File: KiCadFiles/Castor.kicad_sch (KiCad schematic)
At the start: 0 parts

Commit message: Update KiCad project files for Castor: added 3D viewports, IPC2581 settings, and enhanced ERC configurations. Updated schematic with new USB-C and audio jack components, including detailed properties and footprints. Improved net settings and added additional components for better functionality.
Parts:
- added C1, C10, C11, C12, C14, C2, C3, C4, C8, C9: 100nF, Capacitor_SMD:C_0402_1005Metric, symbol Device:C
- added C13, C5: 10uF, Capacitor_SMD:C_0402_1005Metric, symbol Device:C
- added C15, C16, C6, C7: 1uF, Capacitor_SMD:C_0402_1005Metric, symbol Device:C
- added F1, F2: 500mA, Fuse:Fuse_1206_3216Metric, symbol Device:Polyfuse_Small
- added J1, J2: USB_C_Receptacle_USB2.0_14P, Connector_USB:USB_C_Receptacle_HRO_TYPE-C-31-M-12, symbol Connector:USB_C_Receptacle_USB2.0_14P
- added J3: TRRS-L, Connector_Audio:Jack_3.5mm_PJ320E_Horizontal, symbol Connector_Audio:AudioJack4
- added J4: TRRS-R, Connector_Audio:Jack_3.5mm_PJ320E_Horizontal, symbol Connector_Audio:AudioJack4
- added R1, R2, R3, R5: 5.1k, Resistor_SMD:R_0402_1005Metric, symbol Device:R
- added R4, R6: 10k, Resistor_SMD:R_0402_1005Metric, symbol Device:R
- added SW1, SW2, SW3, SW4: SW_DPST_x2, Button_Switch_SMD:SW_Push_1P1T_XKB_TS-1187A, symbol Switch:SW_DPST_x2
- added U1, U5: XC6206PxxxMR, Package_TO_SOT_SMD:SOT-23-3, symbol Regulator_Linear:XC6206PxxxMR
- added U2, U4: STM32F072CBTx, Package_QFP:LQFP-48_7x7mm_P0.5mm, symbol MCU_ST_STM32F0:STM32F072CBTx
- added U3, U6: SRV05-4, Package_TO_SOT_SMD:SOT-23-6, symbol Power_Protection:SRV05-4
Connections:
- new net: J2.A5 (CC1), R5.1
- new net: J2.B5 (CC2), R3.1
- new net: J1.B5 (CC2), R1.1
- new net: J1.A5 (CC1), R2.1
- new net +3V3: C1.1, C10.1, C11.1, C12.1, C13.1, C16.1, C2.1, C3.1, C4.1, C5.1, C7.1, C9.1, J3.S, J4.S, SW2.2 (B), SW4.2 (B), U1.2 (VO), U2.1 (VBAT), U2.24 (VDD), U2.36 (VDDIO2), U2.48 (VDD), U2.9 (VDDA), U4.1 (VBAT), U4.24 (VDD), U4.36 (VDDIO2), U4.48 (VDD), U4.9 (VDDA), U5.2 (VO)
- new net +5V: C15.1, C6.1, F1.2, F2.2, U1.3 (VI), U3.5 (VP), U5.3 (VI), U6.5 (VP)
- new net BOOT-1: R4.1, R6.1, SW2.1 (A), SW4.1 (A), U2.44 (BOOT0), U4.44 (BOOT0)
- new net DN: J1.A7 (D-), J1.B7 (D-), J2.A7 (D-), J2.B7 (D-), U2.32 (PA11), U3.4 (IO3), U4.32 (PA11), U6.4 (IO3)
- new net DP: J1.A6 (D+), J1.B6 (D+), J2.A6 (D+), J2.B6 (D+), U2.33 (PA12), U3.6 (IO4), U4.33 (PA12), U6.6 (IO4)
- new net GND: C1.2, C10.2, C11.2, C12.2, C13.2, C14.2, C15.2, C16.2, C2.2, C3.2, C4.2, C5.2, C6.2, C7.2, C8.2, C9.2, J1.A1 (GND), J1.A12 (GND), J1.B1 (GND), J1.B12 (GND), J2.A1 (GND), J2.A12 (GND), J2.B1 (GND), J2.B12 (GND), J3.R2, J4.R2, R1.2, R2.2, R3.2, R4.2, R5.2, R6.2, SW1.2 (B), SW3.2 (B), U1.1 (GND), U2.23 (VSS), U2.35 (VSS), U2.47 (VSS), U2.8 (VSSA), U3.2 (VN), U4.23 (VSS), U4.35 (VSS), U4.47 (VSS), U4.8 (VSSA), U5.1 (GND), U6.2 (VN)
- new net GNDREF: J1.S1 (SHIELD), J2.S1 (SHIELD)
- new net RST-1: C14.1, C8.1, SW1.1 (A), SW3.1 (A), U2.7 (NRST), U4.7 (NRST)
- new net USART2_RX: J3.R1, J4.T, U2.13 (PA3), U4.13 (PA3)
- new net USART2_TX: J3.T, J4.R1, U2.12 (PA2), U4.12 (PA2)
- new net VBUS: F1.1, F2.1, J1.A4 (VBUS), J1.A9 (VBUS), J1.B4 (VBUS), J1.B9 (VBUS), J2.A4 (VBUS), J2.A9 (VBUS), J2.B4 (VBUS), J2.B9 (VBUS)
- no-connect marks 0 -> 6
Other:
- note added: "Boot Switch"
- note added: "Decoupling Capacitors"
- note added: "ESD Protect"
- note added: "Left"
- note added: "MCU STM32F072CBT6"
- note added: "Regulator XC6206 5V-3.3V"
- note added: "Reset Switch"
- note added: "Right"
- note added: "TRRS-Left(Transmitter)"
- note added: "TRRS-Right(Receiver)"
- note added: "USB-C"

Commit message: Enhance KiCad project files for Castor: updated PCB layout with detailed layer configurations, added new components including a 1N4148WS diode with properties, and improved schematic with additional user-defined symbols. Introduced new DXF files for edge cuts and user layers, and refined layout JSON for better key positioning.
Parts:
- added D1: 1N4148WS, Diode_SMD:D_SOD-323, symbol Diode:1N4148WS
- added MX1, MX10, MX11, MX12, MX13, MX14, MX15, MX16, MX17, MX18, MX19, MX2, MX20, MX21, MX22, MX23, MX24, MX25, MX26, MX27, MX28, MX29, MX3, MX30, MX31, MX32, MX33, MX34, MX35, MX36, MX37, MX38, MX39, MX4, MX40, MX41, MX42, MX5, MX6, MX7, MX8, MX9: ulp_mx_SW_solder, My-Fi Footprints:SW_MX_ULP_1u_Plate, symbol PCM_marbastlib-choc:choc_v1_SW_solder
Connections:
- net GND: now also MX1.2, MX10.2, MX11.2, MX12.2, MX13.2, MX14.2, MX15.2, MX16.2, MX17.2, MX18.2, MX19.2, MX2.2, MX20.2, MX21.2, MX22.2, MX23.2, MX24.2, MX25.2, MX26.2, MX27.2, MX28.2, MX29.2, MX3.2, MX30.2, MX31.2, MX32.2, MX33.2, MX34.2, MX35.2, MX36.2, MX37.2, MX38.2, MX39.2, MX4.2, MX40.2, MX41.2, MX42.2, MX5.2, MX6.2, MX7.2, MX8.2, MX9.2
- new net LEFT1: MX9.1
- new net LEFT10: MX11.1
- new net LEFT11: MX16.1
- new net LEFT12: MX17.1
- new net LEFT13: MX33.1
- new net LEFT14: MX34.1
- new net LEFT15: MX27.1
- new net LEFT16: MX23.1
- new net LEFT17: MX28.1
- new net LEFT18: MX29.1
- new net LEFT19: MX37.1
- new net LEFT2: MX10.1
- new net LEFT20: MX39.1
- new net LEFT21: MX41.1
- new net LEFT3: MX3.1
- new net LEFT4: MX1.1
- new net LEFT5: MX4.1
- new net LEFT6: MX5.1
- new net LEFT7: MX21.1
- new net LEFT8: MX22.1
- new net LEFT9: MX15.1
- new net RIGHT22: MX6.1
- new net RIGHT23: MX7.1
- new net RIGHT24: MX2.1
- new net RIGHT25: MX8.1
- new net RIGHT26: MX13.1
- new net RIGHT27: MX14.1
- new net RIGHT28: MX18.1
- new net RIGHT29: MX19.1
- new net RIGHT30: MX12.1
- new net RIGHT31: MX20.1
- new net RIGHT32: MX25.1
- new net RIGHT33: MX26.1
- new net RIGHT34: MX30.1
- new net RIGHT35: MX31.1
- new net RIGHT36: MX24.1
- new net RIGHT37: MX32.1
- new net RIGHT38: MX35.1
- new net RIGHT39: MX36.1
- new net RIGHT40: MX42.1
- new net RIGHT41: MX40.1
- new net RIGHT42: MX38.1

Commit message: Refactor KiCad project files for Castor: updated PCB layout with new component footprints and adjusted positions for resistors and capacitors. Removed obsolete audio jack symbol from schematic and added new power symbols for +3V3 and GND. Enhanced project configuration with updated track and via dimensions for improved design flexibility.
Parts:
- removed J3: TRRS-L, Connector_Audio:Jack_3.5mm_PJ320E_Horizontal, symbol Connector_Audio:AudioJack4
- removed J4: TRRS-R, Connector_Audio:Jack_3.5mm_PJ320E_Horizontal, symbol Connector_Audio:AudioJack4
- added J5, J6: USB_C_Receptacle_USB2.0_14P, Connector_USB:USB_C_Receptacle_HRO_TYPE-C-31-M-12, symbol Connector:USB_C_Receptacle_USB2.0_14P
- added R7, R8: 5.1k, Resistor_SMD:R_0402_1005Metric, symbol Device:R
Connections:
- net +3V3: now also J5.A4 (VBUS), J5.A9 (VBUS), J5.B4 (VBUS), J5.B9 (VBUS), J6.A4 (VBUS), J6.A9 (VBUS), J6.B4 (VBUS), J6.B9 (VBUS), R7.2
- net GND: now also J5.A1 (GND), J5.A12 (GND), J5.B1 (GND), J5.B12 (GND), J5.S1 (SHIELD), J6.A1 (GND), J6.A12 (GND), J6.B1 (GND), J6.B12 (GND), J6.S1 (SHIELD), R8.2
- net USART2_RX: now also J5.A6 (D+), J5.B6 (D+), J6.A7 (D-), J6.B7 (D-)
- net USART2_TX: now also J5.A7 (D-), J5.B7 (D-), J6.A6 (D+), J6.B6 (D+)
- net HAND_L: now reaches U2.38 (PA15)
- net HAND_L: now also R7.1
- net HAND_R: now reaches U4.38 (PA15)
- net HAND_R: now also R8.1
- no-connect marks 6 -> 10
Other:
- note added: "Left Handness"
- note added: "Right Handness"
- note removed: "TRRS-Left(Transmitter)"
- note removed: "TRRS-Right(Receiver)"
- moved on the sheet: C1, C10, C11, C12, C13, C2, C3, C4, C5, C9, F1, F2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

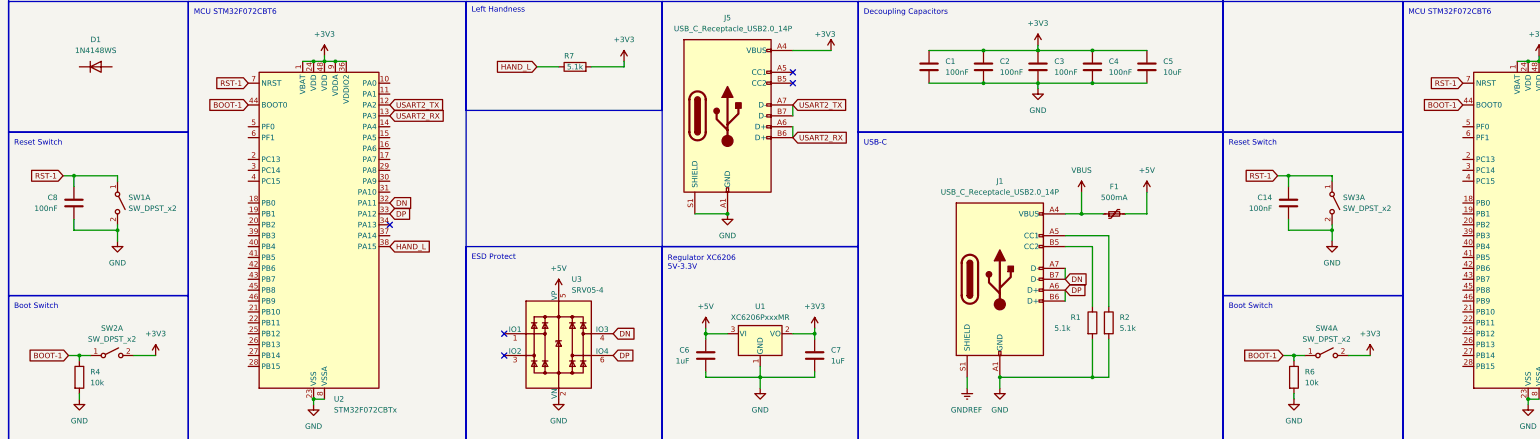
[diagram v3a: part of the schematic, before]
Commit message: Update KiCad project files for Castor: added new global labels for RST and BOOT signals in the schematic, adjusted their positions, and removed obsolete labels. Updated PCB layout with new net connections and refined component placements for improved design clarity.
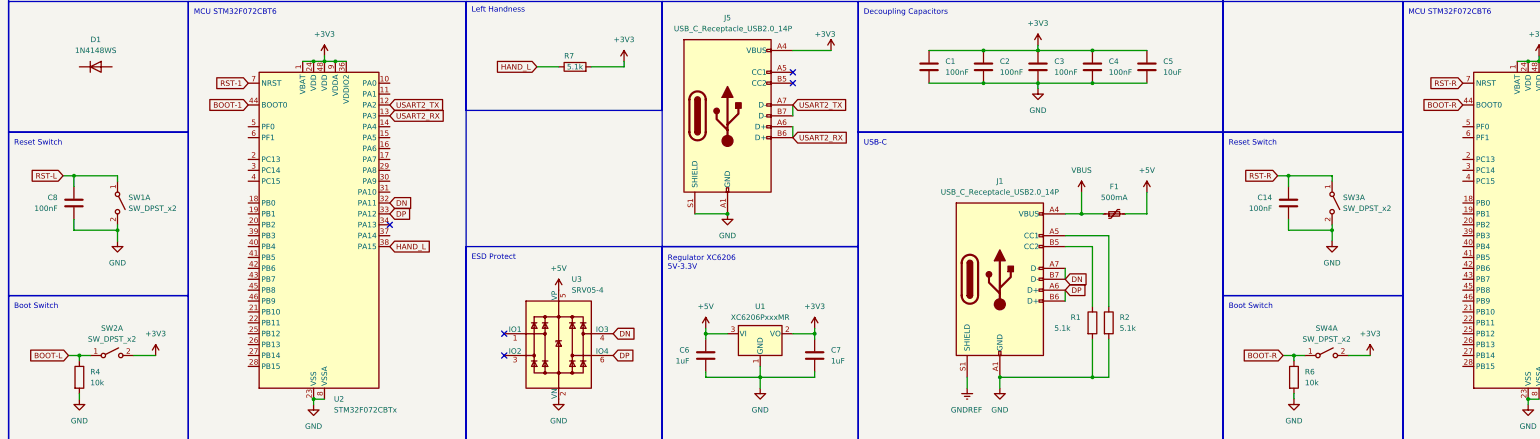
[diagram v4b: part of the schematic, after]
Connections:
- net BOOT-1: no longer R4.1, R6.1, SW2.1 (A), SW4.1 (A), U4.44 (BOOT0)
- net RST-1: no longer C14.1, C8.1, SW1.1 (A), SW3.1 (A), U4.7 (NRST)
- new net BOOT-L: R4.1, SW2.1 (A)
- new net BOOT-R: R6.1, SW4.1 (A), U4.44 (BOOT0)
- new net RST-L: C8.1, SW1.1 (A)
- new net RST-R: C14.1, SW3.1 (A), U4.7 (NRST)

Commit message: updated PCB layout by rearranging net connections and correcting net labels for improved clarity. Added new global labels for BOOT and RST signals in the schematic while removing obsolete labels. Enhanced design consistency across components and connections.
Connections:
- net BOOT-1 is gone; now on net BOOT-L: U2.44 (BOOT0)
- net RST-1 is gone; now on net RST-L: U2.7 (NRST)

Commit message: Update KiCad project files for Castor: added new DRC exclusions in the project configuration, adjusted solder mask clearance, and refined global labels in the schematic for improved clarity. Updated PCB layout with corrected net connections and enhanced design consistency across components.
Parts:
- removed D1: 1N4148WS, Diode_SMD:D_SOD-323, symbol Diode:1N4148WS
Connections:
- net LEFT1: now also U2.45 (PB8)
- net LEFT10: now also U2.3 (PC14)
- net LEFT11: now also U2.2 (PC13)
- net LEFT12: now also U2.46 (PB9)
- net LEFT13: now also U2.19 (PB1)
- net LEFT14: now also U2.18 (PB0)
- net LEFT15: now also U2.17 (PA7)
- net LEFT16: now also U2.16 (PA6)
- net LEFT17: now also U2.15 (PA5)
- net LEFT18: now also U2.14 (PA4)
- net LEFT19: now also U2.20 (PB2)
- net LEFT2: now also U2.43 (PB7)
- net LEFT20: now also U2.21 (PB10)
- net LEFT21: now also U2.22 (PB11)
- net LEFT3: now also U2.42 (PB6)
- net LEFT4: now also U2.41 (PB5)
- net LEFT5: now also U2.40 (PB4)
- net LEFT6: now also U2.39 (PB3)
- net LEFT7: now also U2.6 (PF1)
- net LEFT8: now also U2.5 (PF0)
- net LEFT9: now also U2.4 (PC15)
- net RIGHT22: now also U4.43 (PB7)
- net RIGHT23: now also U4.42 (PB6)
- net RIGHT24: now also U4.41 (PB5)
- net RIGHT25: now also U4.40 (PB4)
- net RIGHT26: now also U4.39 (PB3)
- net RIGHT27: now also U4.37 (PA14)
- net RIGHT28: now also U4.31 (PA10)
- net RIGHT29: now also U4.30 (PA9)
- net RIGHT30: now also U4.29 (PA8)
- net RIGHT31: now also U4.28 (PB15)
- net RIGHT32: now also U4.27 (PB14)
- net RIGHT33: now also U4.26 (PB13)
- net RIGHT34: now also U4.22 (PB11)
- net RIGHT35: now also U4.21 (PB10)
- net RIGHT36: now also U4.20 (PB2)
- net RIGHT37: now also U4.19 (PB1)
- net RIGHT38: now also U4.18 (PB0)
- net RIGHT39: now also U4.17 (PA7)
- net RIGHT40: now also U4.14 (PA4)
- net RIGHT41: now also U4.15 (PA5)
- net RIGHT42: now also U4.16 (PA6)
